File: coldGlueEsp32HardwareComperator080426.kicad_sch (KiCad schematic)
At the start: 77 parts, among them CN1 KF243-5.0-2P, CN2 KF243-5.0-2P, CN3 KF243-5.0-2P, CN4 KF243-5.0-2P, CN5 KF243-5.0-2P, CN6 KF243-5.0-2P, CN7 KF243-5.0-2P, CN9 KF243-5.0-4P, J1 Female Header 1x22, J2 Female Header 1x22, Q1 SQM120P10-10m1L, U1 DRV8262DDWR, U10 INA240A2DR, U11 INA240A2DR, U2 DRV8262DDWR, U3 ESP32-S3-DEVKITC-1-N8R8, U5 6N137, U6 INA240A2DR, U7 INA240A2DR, U8 K7805-1000R3_C2992391, U9 TLP291-4(V4GBTPE)

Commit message: complete adding hardware comerator to schematics
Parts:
- added C11, C12, C13, C14, C15, C22, C23: 100nf 50v, Capacitor_SMD:C_0603_1608Metric, symbol Device:C
- added R10, R21, R22, R23: 10k, Resistor_SMD:R_0603_1608Metric, symbol Device:R
- added U12: LM339, Package_SO : SOIC-14_3.9x8.7mm_P1.27mm, symbol Comparator:LM339
- added U13, U14, U15, U16: 74LVC1G157GV,125, easyeda2kicad:TSOP-6_L3.0-W1.5-P0.95-LS2.8-BR, symbol easyeda2kicad:74LVC1G157GV,125
- added U4: MCP4728, Package_SO:MSOP-10_3x3mm_P0.5mm, symbol Analog_DAC:MCP4728
- R11: value 330r -> 100r; LCSC part C23138 -> (none)
- R7: value 100k -> 33k; LCSC part C25611 -> (none)
- R8: value 47k -> 100k; LCSC part C17713 -> C25611
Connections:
- net +3V3: now also R1.2, C12.2, C14.1, C15.1, C22.1, C23.1, R10.2, R21.2, R22.2, R23.2, U13.5 (VCC), U14.5 (VCC), U15.5 (VCC), U16.5 (VCC), U4.1 (VDD)
- net +5V: now also C13.2, U12.3 (V+); no longer U5.7 (EN), U5.8 (VCC)
- net GND: now also C11.2, C12.1, C13.1, C14.2, C15.2, C22.2, C23.2, U12.12 (V-), U13.2 (GND), U14.2 (GND), U15.2 (GND), U16.2 (GND), U4.10 (VSS), U4.4 (~{LDAC}); no longer R1.2
- net Input_1_24v: now also U3.J3_4 (GPIO1); no longer U3.J3_9 (MTCK/GPIO39)
- net Input_2_24v: now also U3.J3_5 (GPIO2); no longer U3.J3_8 (MTDO/GPIO40)
- net Input_3_24v: now also U3.J1_4 (GPIO4); no longer U3.J1_17 (GPIO11)
- net Input_4_24v: now also U3.J1_5 (GPIO5); no longer U3.J1_18 (GPIO12)
- net U1_IN1: now also U3.J1_6 (GPIO6); no longer U3.J1_4 (GPIO4)
- net U1_IN2: now also U13.4 (Y); no longer U3.J1_5 (GPIO5)
- net U1_IN3: now also U3.J1_7 (GPIO7); no longer U3.J1_6 (GPIO6)
- net U1_IN4: now also U14.4 (Y); no longer U3.J1_7 (GPIO7)
- net U1_OUT4: now also CN3.2; no longer CN3.1
- net U2_IN2: now also U15.4 (Y); no longer U3.J1_9 (GPIO16)
- net U2_IN3: now also U3.J1_9 (GPIO16); no longer U3.J1_10 (GPIO17)
- net U2_IN4: now also U16.4 (Y); no longer U3.J1_11 (GPIO18)
- net U2_OUT4: now also CN5.2; no longer CN5.1
- net nFAULT: now also U3.J3_9 (MTCK/GPIO39); no longer U3.J1_19 (GPIO13)
- net nSLEEP: no longer U3.J1_12 (GPIO8)
- net MUX_3_SELECT: now reaches U3.J1_20 (GPIO14)
- net MUX_3_SELECT: now also U15.6 (S)
- net Gun4Interrupt: now reaches U3.J3_10 (GPIO38)
- net Gun4Interrupt: now also R23.1, U12.14, U16.1 (I1)
- net MUX_4_SELECT: now reaches U3.J3_16 (GPIO48)
- net MUX_4_SELECT: now also U16.6 (S)
- net I2C_SCL: now reaches U3.J3_6 (MTMS/GPIO42)
- net I2C_SCL: now also U4.2 (SCL)
- net I2C_SDA: now reaches U3.J3_7 (MTDI/GPIO41)
- net I2C_SDA: now also U4.3 (SDA)
- net pure5V: now reaches C17.1, D14.2 (A), U8.3 (+VO)
- net pure5V: now also U5.7 (EN), U5.8 (VCC), C11.1
- net at R20.1, U11.1 (IN-): now also CN5.1; no longer CN5.2
- net at R18.1, U7.1 (IN-): now also CN3.1; no longer CN3.2
- net Gun1Vref renamed Gun1_Sense
- net Gun1_Sense: now also U12.5 (+); no longer U3.J3_4 (GPIO1)
- net Gun2Vref renamed Gun2_Sense
- net Gun2_Sense: now also U12.7 (+); no longer U3.J3_5 (GPIO2)
- net Gun3Vref renamed Gun3_Sense
- net Gun3_Sense: now also U12.11 (+); no longer U3.J1_15 (GPIO9)
- net Gun4Vref renamed Gun4_Sense
- net Gun4_Sense: now also U12.9 (+); no longer U3.J1_16 (GPIO10)
- net Input_0_5v renamed ENCODER
- net ENCODER: now also U3.J3_8 (MTDO/GPIO40); no longer U3.J3_18 (GPIO21)
- new net: U12.6 (-), U4.7 (VOUTB)
- new net: U12.8 (-), U4.9 (VOUTD)
- new net: U12.4 (-), U4.6 (VOUTA)
- new net: U12.10 (-), U4.8 (VOUTC)
- new net Gun1Interrupt: R10.1, U12.2, U13.1 (I1), U3.J1_18 (GPIO12)
- new net Gun2Interrupt: R21.1, U12.1, U14.1 (I1), U3.J1_19 (GPIO13)
- new net Gun3Interrupt: R22.1, U12.13, U15.1 (I1), U3.J3_18 (GPIO21)
- new net MUX_1_IN0: U13.3 (I0), U3.J1_12 (GPIO8)
- new net MUX_1_SELECT: U13.6 (S), U3.J1_16 (GPIO10)
- new net MUX_2_IN0: U14.3 (I0), U3.J1_15 (GPIO9)
- new net MUX_2_SELECT: U14.6 (S), U3.J1_17 (GPIO11)
- new net MUX_3_IN0: U15.3 (I0), U3.J1_10 (GPIO17)
- new net MUX_4_IN0: U16.3 (I0), U3.J1_11 (GPIO18)
- no-connect marks 37 -> 32
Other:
- moved on the sheet: C10, C18, C19, C20, C21, C3, C4, C5, C6, C7, C8, C9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

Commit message: wiring headers and remove esp from board before routing
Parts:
- J1: footprint (none) -> Connector_PinSocket_2.54mm:PinSocket_1x22_P2.54mm_Vertical
- J3: renamed from J2; footprint (none) -> Connector_PinSocket_2.54mm:PinSocket_1x22_P2.54mm_Vertical
- R12, R13, R15, R16: value 2.2k -> 4.7k; LCSC part C17948 -> (none)
- U10, U11, U6, U7: LCSC Part (none) -> C2060768
- U12: footprint Package_SO : SOIC-14_3.9x8.7mm_P1.27mm -> Package_SO:SOIC-14_3.9x8.7mm_P1.27mm
- U3: LCSC part (none) -> 2X C7499337 - Female Header 1x22
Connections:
- net MUX_1_IN0 is gone; now on net J1_12: U13.3 (I0), U3.J1_12 (GPIO8)
- net MUX_1_SELECT is gone; now on net J1_16: U13.6 (S), U3.J1_16 (GPIO10)
- net MUX_2_IN0 is gone; now on net J1_15: U14.3 (I0), U3.J1_15 (GPIO9)
- net MUX_2_SELECT is gone; now on net J1_17: U14.6 (S), U3.J1_17 (GPIO11)
- net MUX_3_IN0 is gone; now on net J1_10: U15.3 (I0), U3.J1_10 (GPIO17)
- net MUX_3_SELECT is gone; now on net J1_20: U15.6 (S), U3.J1_20 (GPIO14)
- net MUX_4_IN0 is gone; now on net J1_11: U16.3 (I0), U3.J1_11 (GPIO18)
- net MUX_4_SELECT is gone; now on net J3_16: U16.6 (S), U3.J3_16 (GPIO48)
- net U1_IN1 is gone; now on net J1_6: RN1.8 (R1.2), U1.41 (IN1/NFAULT), U3.J1_6 (GPIO6)
- net U1_IN3 is gone; now on net J1_7: RN1.7 (R2.2), U1.39 (RSVD/MODE1), U3.J1_7 (GPIO7)
- net U2_IN1 is gone; now on net J1_8: RN1.6 (R3.2), U2.41 (IN1/NFAULT), U3.J1_8 (GPIO15)
- net U2_IN3 is gone; now on net J1_9: RN1.5 (R4.2), U2.39 (RSVD/MODE1), U3.J1_9 (GPIO16)
- net nFAULT is gone; now on net J3_9: R2.1, U1.26 (NFAULT/IN1), U2.26 (NFAULT/IN1), U3.J3_9 (MTCK/GPIO39)
- net +3V3: now also J1.1 (Pin_1), J1.2 (Pin_2)
- net +5V: now also J1.21 (Pin_21)
- net ENCODER: now also J3.8 (Pin_8)
- net GND: now also J1.22 (Pin_22), J3.1 (Pin_1), J3.21 (Pin_21), J3.22 (Pin_22)
- net Gun1Interrupt: now also J1.18 (Pin_18)
- net Gun2Interrupt: now also J1.19 (Pin_19)
- net Gun3Interrupt: now also J3.18 (Pin_18)
- net Gun4Interrupt: now also J3.10 (Pin_10)
- net I2C_SCL: now also J3.6 (Pin_6)
- net I2C_SDA: now also J3.7 (Pin_7)
- net Input_1_24v: now also J3.4 (Pin_4)
- net Input_2_24v: now also J3.5 (Pin_5)
- net Input_3_24v: now also J1.4 (Pin_4)
- net Input_4_24v: now also J1.5 (Pin_5)
- net J1_13: now reaches U3.J1_13 (GPIO3)
- net J1_13: now also J1.13 (Pin_13)
- net J1_14: now reaches U3.J1_14 (GPIO46)
- net J1_14: now also J1.14 (Pin_14)
- net J1_3: now reaches U3.J1_3 (RST)
- net J1_3: now also J1.3 (Pin_3)
- net J3_11: now reaches U3.J3_11 (GPIO37)
- net J3_11: now also J3.11 (Pin_11)
- net J3_12: now reaches U3.J3_12 (GPIO36)
- net J3_12: now also J3.12 (Pin_12)
- net J3_13: now reaches U3.J3_13 (GPIO35)
- net J3_13: now also J3.13 (Pin_13)
- net J3_14: now reaches U3.J3_14 (GPIO0)
- net J3_14: now also J3.14 (Pin_14)
- net J3_15: now reaches U3.J3_15 (GPIO45)
- net J3_15: now also J3.15 (Pin_15)
- net J3_17: now reaches U3.J3_17 (GPIO47)
- net J3_17: now also J3.17 (Pin_17)
- net J3_19: now reaches U3.J3_19 (USB_D+/GPIO20)
- net J3_19: now also J3.19 (Pin_19)
- net J3_2: now reaches U3.J3_2 (U0TXD/GPIO43)
- net J3_2: now also J3.2 (Pin_2)
- net J3_20: now reaches U3.J3_20 (USB_D-/GPIO19)
- net J3_20: now also J3.20 (Pin_20)
- net J3_3: now reaches U3.J3_3 (U0RXD/GPIO44)
- net J3_3: now also J3.3 (Pin_3)
- net J3_16: now reaches J3.16 (Pin_16)
- net J3_9: now reaches J3.9 (Pin_9)
- net J1_10: now reaches J1.10 (Pin_10)
- net J1_11: now reaches J1.11 (Pin_11)
- net J1_12: now reaches J1.12 (Pin_12)
- net J1_15: now reaches J1.15 (Pin_15)
- net J1_16: now reaches J1.16 (Pin_16)
- net J1_17: now reaches J1.17 (Pin_17)
- net J1_20: now reaches J1.20 (Pin_20)
- net J1_6: now reaches J1.6 (Pin_6)
- net J1_7: now reaches J1.7 (Pin_7)
- net J1_8: now reaches J1.8 (Pin_8)
- net J1_9: now reaches J1.9 (Pin_9)
- no-connect marks 32 -> 19
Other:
- moved on the sheet: J1, U3

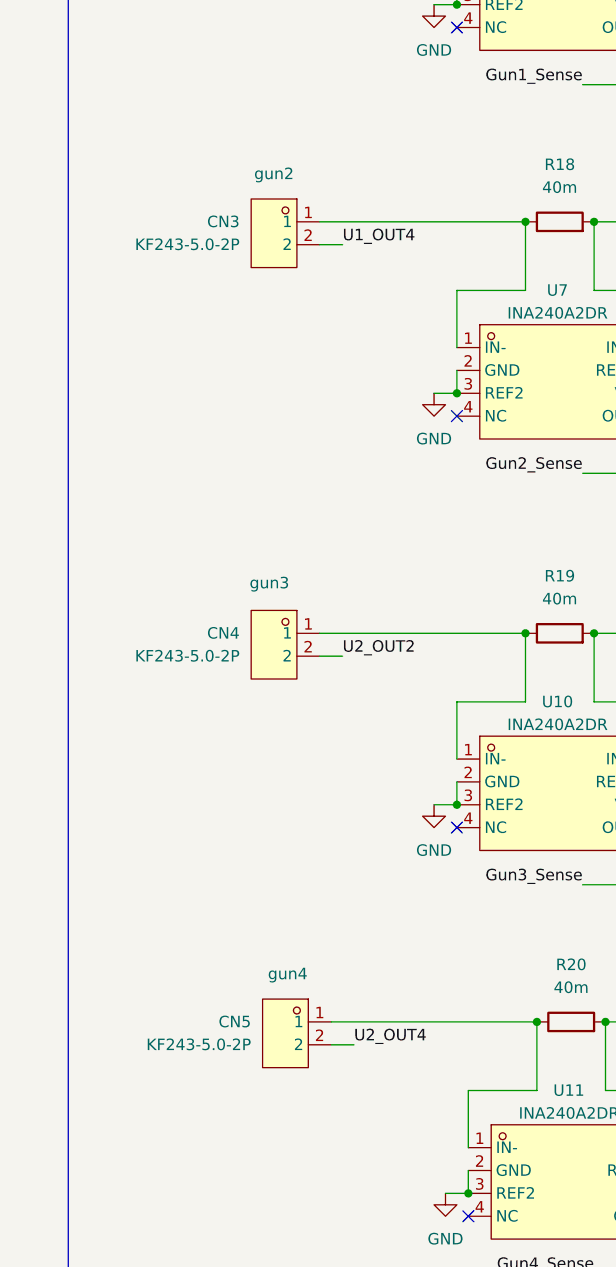
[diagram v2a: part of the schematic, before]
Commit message: CN3,5 fix orientation(before  freerouting)
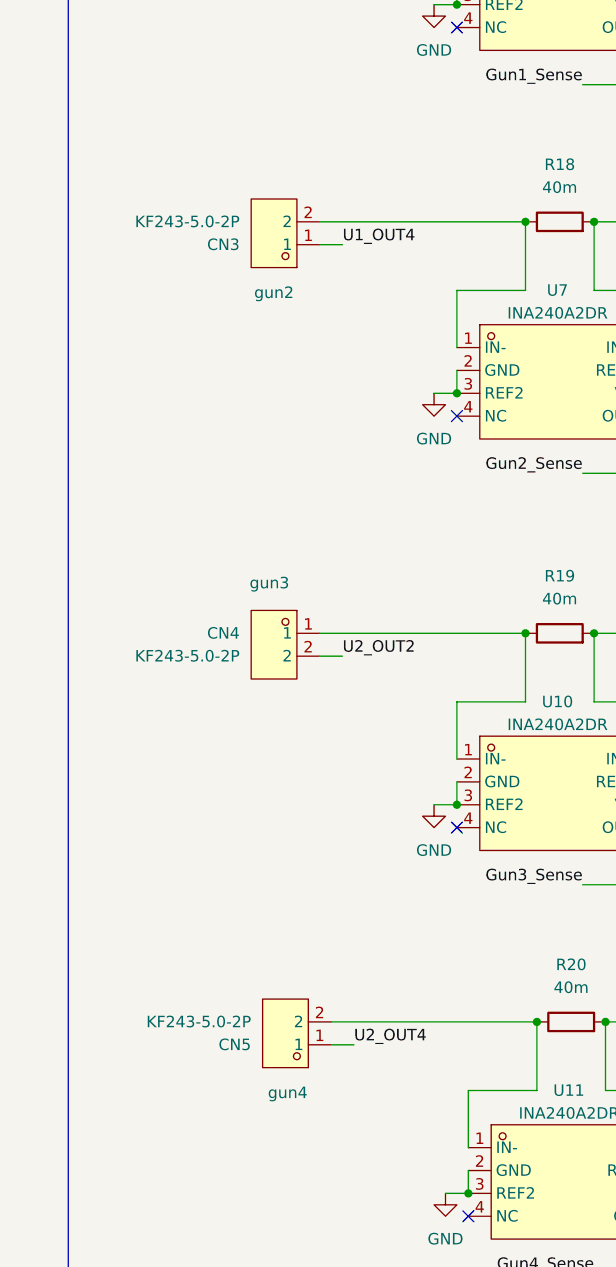
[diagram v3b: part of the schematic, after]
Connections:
- net U1_OUT4: now also CN3.1; no longer CN3.2
- net U2_OUT4: now also CN5.1; no longer CN5.2
- net at R20.1, U11.1 (IN-): now also CN5.2; no longer CN5.1
- net at R18.1, U7.1 (IN-): now also CN3.2; no longer CN3.1
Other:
- moved on the sheet: CN3, CN5

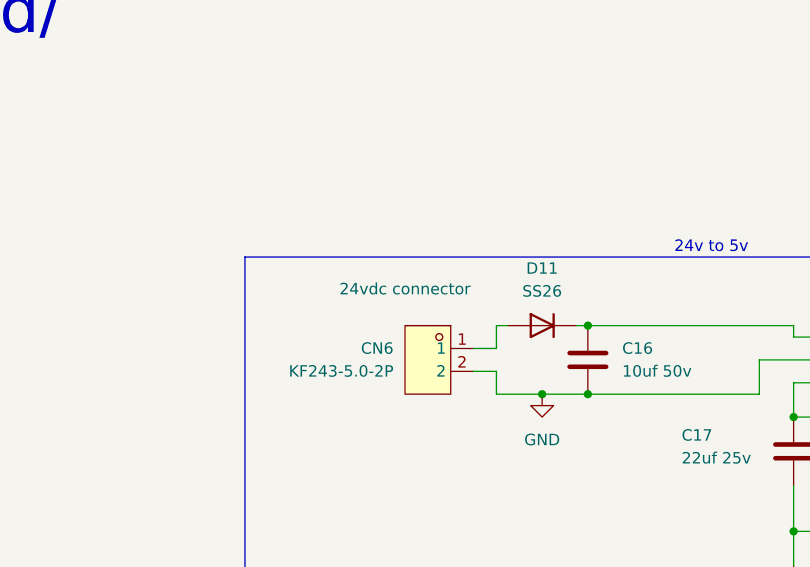
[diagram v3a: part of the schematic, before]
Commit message: complete routing
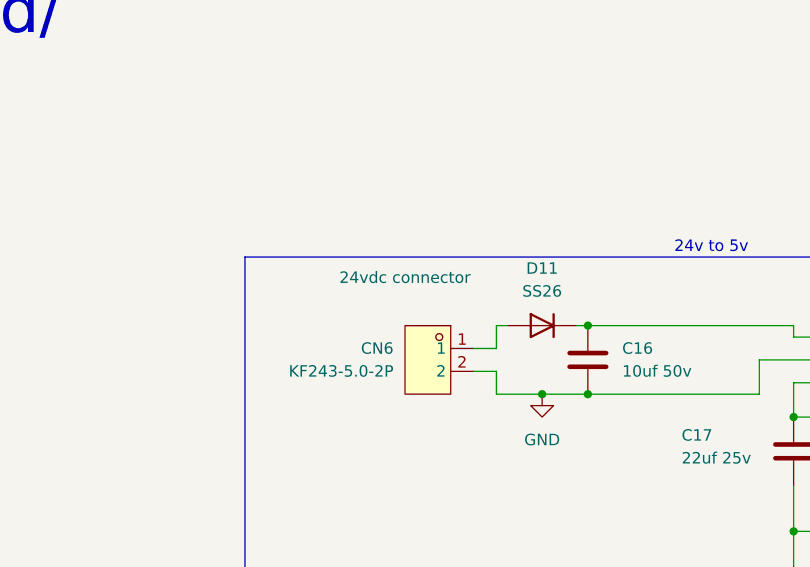
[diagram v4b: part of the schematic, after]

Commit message: all lcsc part numbers collected
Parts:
- R11: LCSC part (none) -> C22775
- R12, R13, R15, R16: LCSC part (none) -> C17936
- R7: LCSC part (none) -> C17633
- U1, U2: LCSC part (none) -> C22427252
- U10, U11, U6, U7: LCSC Part C2060768 -> (none)
- U13, U14, U15, U16: LCSC Part C503437 -> (none); LCSC part (none) -> C503437
- U3: LCSC part 2X C7499337 - Female Header 1x22 -> (none)

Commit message: lcsc collumn renamed all parts in stock now
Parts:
- C1, C2: LCSC (none) -> C507603; LCSC part C42404588 -> (none); LCSC_ALT (none) -> C507603; SEARCH_TERM (none) -> uf680 100v 7.5mm 16mm; original_LCSC_PART (none) -> C42404588
- C10, C11, C12, C13, C14, C15, C22, C23, C6: LCSC (none) -> C14663; LCSC part C14663 -> (none); lcsc C309458 -> (none)
- C16: LCSC (none) -> C13585; LCSC part C13585 -> (none); lcsc C513774 -> (none)
- C17: LCSC (none) -> C12891; LCSC part C12891 -> (none); lcsc C513771 -> (none)
- C18, C19, C20, C21: LCSC (none) -> C14663; LCSC part C14663 -> (none)
- C3, C5, C7, C9: LCSC (none) -> C15849; LCSC part C15849 -> (none); lcsc C106248 -> (none)
- C4, C8: LCSC (none) -> C28233; LCSC part C28233 -> (none); lcsc C113803 -> (none)
- CN1, CN2, CN3, CN4, CN5, CN6, CN7: LCSC (none) -> C475222; LCSC part C475222 -> (none)
- CN9: LCSC (none) -> C475224; LCSC part C475224 -> (none)
- D1, D14: LCSC (none) -> C2480; LCSC part C2480 -> (none)
- D10, D2, D3, D4, D5: LCSC (none) -> C2297; LCSC part C2297 -> (none); lcsc C2297 -> (none)
- D11: LCSC (none) -> C14238; LCSC part C14238 -> (none)
- D12: LCSC (none) -> C2104; LCSC part C2104 -> (none)
- D13: LCSC (none) -> C438115; LCSC part C438115 -> (none)
- D15: LCSC (none) -> C2296; LCSC part C2296 -> (none); lcsc C2297 -> (none)
- D6, D7, D8, D9: LCSC (none) -> C84256; LCSC part C84256 -> (none)
- J1, J3: LCSC (none) -> C7499337; LCSC part C7499337 -> (none); LCSC_ALT (none) -> C47940(40p); SEARCH_TERM (none) -> CONN SOCKET 22POS 2.54mm SINGLE ROW TH; original_LCSC_PART (none) -> C7499337
- Q1: LCSC (none) -> C3281565; LCSC part C3281565 -> (none); LCSC_ALT (none) -> C468007; original_LCSC_PART (none) -> C3281565
- R1, R10, R2, R21, R22, R23: LCSC (none) -> C25804; LCSC part C25804 -> (none); lcsc C84376 -> (none)
- R11: LCSC (none) -> C22775; LCSC part C22775 -> (none)
- R12, R13, R15, R16: LCSC (none) -> C17936; LCSC part C17936 -> (none)
- R14: LCSC (none) -> C21190; LCSC part C21190 -> (none)
- R17, R18, R19, R20: LCSC (none) -> C459685; LCSC part C459685 -> (none); lcsc C500722 -> (none)
- R3, R4, R5, R6: LCSC (none) -> C23186; LCSC part C23186 -> (none)
- R7: LCSC (none) -> C17633; LCSC part C17633 -> (none)
- R8: LCSC (none) -> C25611; LCSC part C25611 -> (none)
- R9: LCSC (none) -> C23179; LCSC part C23179 -> (none)
- RN1: LCSC (none) -> C354986; LCSC part C354986 -> (none); LCSC_ALT (none) -> C25510; original_LCSC_PART (none) -> C354986
- RN2: LCSC (none) -> C107374; LCSC part C107374 -> (none); LCSC_ALT (none) -> C29718; original_LCSC_PART (none) -> C107374
- U1, U2: LCSC (none) -> C22427252; LCSC part C22427252 -> (none)
- U10, U11, U6, U7: LCSC (none) -> C2060768; LCSC part C2060768 -> (none)
- U12: LCSC (none) -> C7948; LCSC part C7948 -> (none)
- U13, U14, U15, U16: LCSC (none) -> C503437; LCSC part C503437 -> (none)
- U4: LCSC (none) -> C478093; LCSC part C478093 -> (none)
- U5: LCSC (none) -> C16496; LCSC part C16496 -> (none)
- U8: LCSC (none) -> C2992391; LCSC part C2992391 -> (none)
- U9: LCSC (none) -> C2848503; LCSC part C2848503 -> (none); original_LCSC_PART (none) -> C2848503
